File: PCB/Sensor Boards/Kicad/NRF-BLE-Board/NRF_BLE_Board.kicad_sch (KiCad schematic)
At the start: 13 parts, among them U1 nRF52805-CAxx, Y1 Crystal

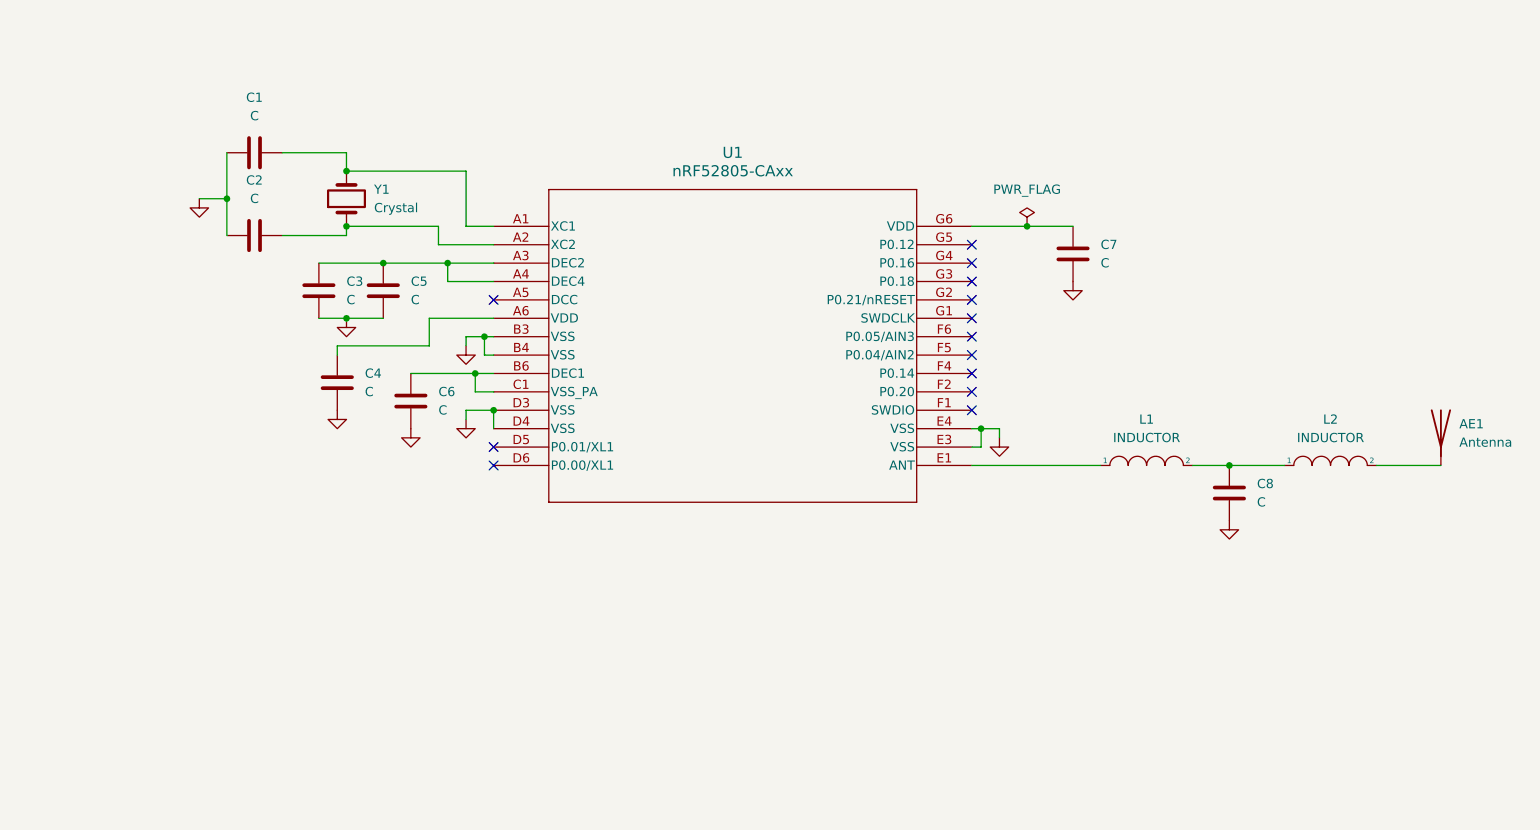
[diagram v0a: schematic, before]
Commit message: Initial placement and routing done
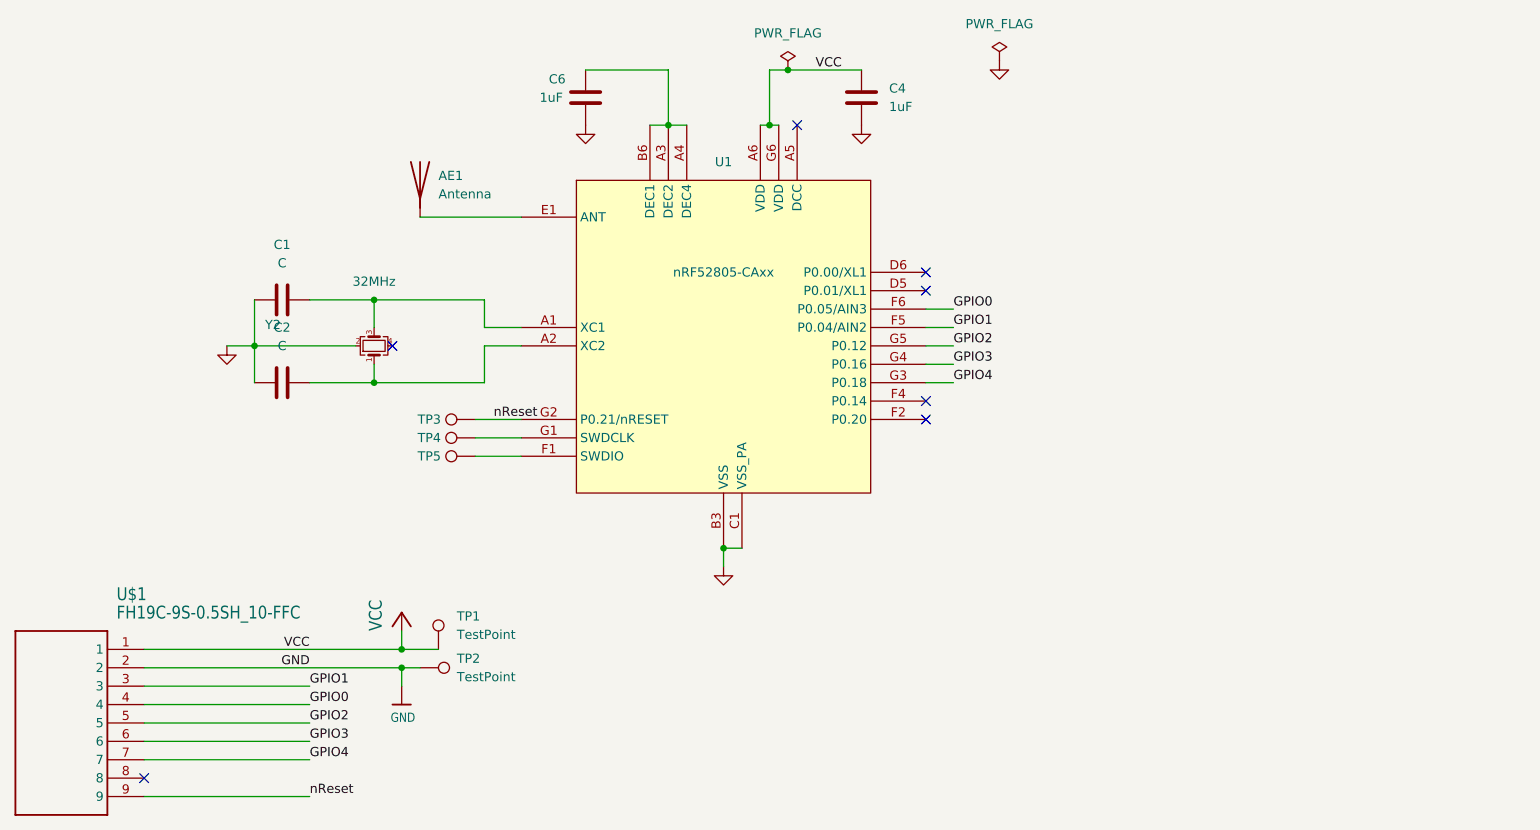
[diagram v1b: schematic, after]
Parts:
- removed C3, C5, C7, C8: C, Capacitor_SMD:C_0201_0603Metric_Pad0.64x0.40mm_HandSolder, symbol Device:C
- removed L1, L2: INDUCTOR, Inductor_SMD:L_0201_0603Metric_Pad0.64x0.40mm_HandSolder, symbol pspice:INDUCTOR
- removed Y1: Crystal, Oscillator:Oscillator_SMD_Abracon_ASCO-4Pin_1.6x1.2mm, symbol Device:Crystal
- added TP1, TP2, TP3, TP4, TP5: TestPoint, TestPoint:TestPoint_Pad_D1.0mm, symbol Connector:TestPoint
- added U$1: FH19C-9S-0.5SH_10-FFC, OSO-SWAB-B1-00 Sensor Watch Accelerometer:FH19C9S05SH10-FFC, symbol OSO-MISC-21-021 Sensor Watch Motion II-eagle-import:FH19C-9S-0.5SH_10-FFC
- added Y2: 32MHz, Crystal:Crystal_SMD_Murata_XRCTD32M000N1P1AR0-4pin_1.2x1.0mm, symbol Device:Crystal_GND24_Small
- AE1: footprint Capacitor_SMD:C_0402_1005Metric -> Capacitor_SMD:C_0402_1005Metric_Pad0.74x0.62mm_HandSolder
- C1, C2: footprint Capacitor_SMD:C_0201_0603Metric_Pad0.64x0.40mm_HandSolder -> Capacitor_SMD:C_0402_1005Metric_Pad0.74x0.62mm_HandSolder
- C4, C6: value C -> 1uF; footprint Capacitor_SMD:C_0201_0603Metric_Pad0.64x0.40mm_HandSolder -> Capacitor_SMD:C_0402_1005Metric_Pad0.74x0.62mm_HandSolder
- U1: footprint Package_CSP:NRF_WLCSP-28_2.482X2.464_NOR -> Package_CSP:NRF_WLCSP-28_2.48x2.64mm_P0.4mm
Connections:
- net GND: now also U1.C1 (VSS_PA), TP2.1, U$1.2, Y2.2
- net VCC: now reaches C4.1, U1.A6 (VDD)
- net VCC: now also U1.G6 (VDD), TP1.1, U$1.1
- net at C2.2, U1.A2 (XC2): now also Y2.1
- net at C1.2, U1.A1 (XC1): now also Y2.3
- net at U1.A3 (DEC2), U1.A4 (DEC4): now also C6.1, U1.B6 (DEC1)
- net at U1.E1 (ANT): now also AE1.1 (A)
- net at U1.F1 (SWDIO): now also TP5.1
- net GPIO1: now reaches U1.F5 (P0.04/AIN2)
- net GPIO1: now also U$1.3
- net GPIO0: now reaches U1.F6 (P0.05/AIN3)
- net GPIO0: now also U$1.4
- net at U1.G1 (SWDCLK): now also TP4.1
- net nReset: now reaches U1.G2 (P0.21/nRESET)
- net nReset: now also TP3.1, U$1.9
- net GPIO4: now reaches U1.G3 (P0.18)
- net GPIO4: now also U$1.7
- net GPIO3: now reaches U1.G4 (P0.16)
- net GPIO3: now also U$1.6
- net GPIO2: now reaches U1.G5 (P0.12)
- net GPIO2: now also U$1.5
- no-connect marks 13 -> 7
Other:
- moved on the sheet: AE1, C1, C2, C4, C6

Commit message: Routing completed
order placed at OSH Park with this gerber.
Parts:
- removed TP1, TP2, TP4, TP5: TestPoint, TestPoint:TestPoint_Pad_D1.0mm, symbol Connector:TestPoint
- added J1: Conn_01x04, TestPoint:TestPoint_4Pads_Pitch1.27mm, symbol Connector_Generic:Conn_01x04
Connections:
- net GND: now also J1.2 (Pin_2)
- net VCC: now also J1.1 (Pin_1)
- net SWDIO: now reaches U1.F1 (SWDIO)
- net SWDIO: now also J1.3 (Pin_3)
- net SWDCLK: now reaches U1.G1 (SWDCLK)
- net SWDCLK: now also J1.4 (Pin_4)
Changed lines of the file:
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@@
   (junction (at 93.98 107.95) (diameter 0) (color 0 0 0 0)
-  )
-  (junction (at 97.79 147.32) (diameter 0) (color 0 0 0 0)
-  )
-  (junction (at 97.79 144.78) (diameter 0) (color 0 0 0 0)
   )
   (junction (at 93.98 96.52) (diameter 0) (color 0 0 0 0)
@@
     (stroke (width 0) (type default))
   )
-  (wire (pts (xy 107.95 118.11) (xy 114.3 118.11))
+  (wire (pts (xy 100.33 118.11) (xy 114.3 118.11))
     (stroke (width 0) (type default))
   )
@@
     (stroke (width 0) (type default))
   )
+  (wire (pts (xy 69.85 120.65) (xy 74.93 120.65))
+    (stroke (width 0) (type default))
+  )
   (wire (pts (xy 85.09 165.1) (xy 62.23 165.1))
     (stroke (width 0) (type default))
@@
     (stroke (width 0) (type default))
   )
-  (wire (pts (xy 97.79 147.32) (xy 100.33 147.32))
-    (stroke (width 0) (type default))
-  )
   (wire (pts (xy 97.79 147.32) (xy 62.23 147.32))
     (stroke (width 0) (type default))
@@
     (stroke (width 0) (type default))
   )
+  (wire (pts (xy 69.85 118.11) (xy 76.2 118.11))
+    (stroke (width 0) (type default))
+  )
   (wire (pts (xy 134.62 72.39) (xy 137.16 72.39))
     (stroke (width 0) (type default))
@@
     (stroke (width 0) (type default))
   )
-  (wire (pts (xy 107.95 115.57) (xy 114.3 115.57))
+  (wire (pts (xy 100.33 115.57) (xy 114.3 115.57))
     (stroke (width 0) (type default))
   )
@@
     (stroke (width 0) (type default))
   )
-  (wire (pts (xy 102.87 144.78) (xy 97.79 144.78))
-    (stroke (width 0) (type default))
-  )
   (wire (pts (xy 77.47 102.87) (xy 77.47 107.95))
     (stroke (width 0) (type default))
   )
+  (wire (pts (xy 69.85 115.57) (xy 76.2 115.57))
+    (stroke (width 0) (type default))
+  )
   (wire (pts (xy 85.09 107.95) (xy 93.98 107.95))
     (stroke (width 0) (type default))
@@
     (stroke (width 0) (type default))
   )
+  (wire (pts (xy 69.85 123.19) (xy 74.93 123.19))
+    (stroke (width 0) (type default))
+  )
   (wire (pts (xy 148.59 72.39) (xy 149.86 72.39))
     (stroke (width 0) (type default))
@@
     (effects (font (size 1.27 1.27)) (justify left bottom))
   )
+  (label "VCC" (at 74.93 123.19 180) (fields_autoplaced)
+    (effects (font (size 1.2446 1.2446)) (justify right bottom))
+  )
   (label "GPIO1" (at 85.09 149.86 0) (fields_autoplaced)
     (effects (font (size 1.27 1.27)) (justify left bottom))
@@
     (effects (font (size 1.27 1.27)) (justify left bottom))
   )
+  (label "SWDIO" (at 100.33 118.11 0) (fields_autoplaced)
+    (effects (font (size 1 1)) (justify left bottom))
+  )
+  (label "SWDCLK" (at 100.33 115.57 0) (fields_autoplaced)
+    (effects (font (size 1 1)) (justify left bottom))
+  )
   (label "GPIO0" (at 173.99 97.79 0) (fields_autoplaced)
     (effects (font (size 1.27 1.27)) (justify left bottom))
+  )
+  (label "SWDIO" (at 76.2 118.11 180) (fields_autoplaced)
+    (effects (font (size 1 1)) (justify right bottom))
+  )
+  (label "GND" (at 74.93 120.65 180) (fields_autoplaced)
+    (effects (font (size 1.2446 1.2446)) (justify right bottom))
   )
   (label "nReset" (at 85.09 165.1 0) (fields_autoplaced)
@@
   (label "GND" (at 85.09 147.32 180) (fields_autoplaced)
     (effects (font (size 1.2446 1.2446)) (justify right bottom))
+  )
+  (label "SWDCLK" (at 76.2 115.57 180) (fields_autoplaced)
+    (effects (font (size 1 1)) (justify right bottom))
   )
   (label "GPIO0" (at 85.09 152.4 0) (fields_autoplaced)
@@
     )
   )
-  (symbol (lib_id "Connector:TestPoint") (at 100.33 147.32 270) (unit 1)
-    (in_bom yes) (on_board yes) (dnp no) (fields_autoplaced)
-    (property "Reference" "TP2" (at 105.41 146.05 90)
-      (effects (font (size 1.27 1.27)) (justify left))
-    )
-    (property "Value" "TestPoint" (at 105.41 148.59 90)
-      (effects (font (size 1.27 1.27)) (justify left))
-    )
-    (property "Footprint" "TestPoint:TestPoint_Pad_D1.0mm" (at 100.33 152.4 0)
-      (effects (font (size 1.27 1.27)) hide)
-    )
-    (property "Datasheet" "~" (at 100.33 152.4 0)
-      (effects (font (size 1.27 1.27)) hide)
-    )
-    (pin "1")
-    (instances
-      (project "NRF_BLE_Board"
-        (path "/34b18e33-c413-4b44-9f16-855bb8aeab29"
-          (reference "TP2") (unit 1)
-        )
-      )
-    )
-  )
   (symbol (lib_id "power:PWR_FLAG") (at 151.13 64.77 0) (unit 1)
     (in_bom yes) (on_board yes) (dnp no) (fields_autoplaced)
@@
         (path "/34b18e33-c413-4b44-9f16-855bb8aeab29"
           (reference "#FLG01") (unit 1)
-        )
-      )
-    )
-  )
-  (symbol (lib_id "Connector:TestPoint") (at 107.95 118.11 90) (unit 1)
-    (in_bom yes) (on_board yes) (dnp no)
-    (property "Reference" "TP5" (at 101.6 118.11 90)
-      (effects (font (size 1.27 1.27)))
-    )
-    (property "Value" "TestPoint" (at 104.648 115.57 90)
-      (effects (font (size 1.27 1.27)) hide)
-    )
-    (property "Footprint" "TestPoint:TestPoint_Pad_D1.0mm" (at 107.95 113.03 0)
-      (effects (font (size 1.27 1.27)) hide)
-    )
-    (property "Datasheet" "~" (at 107.95 113.03 0)
-      (effects (font (size 1.27 1.27)) hide)
-    )
-    (pin "1")
-    (instances
-      (project "NRF_BLE_Board"
-        (path "/34b18e33-c413-4b44-9f16-855bb8aeab29"
-          (reference "TP5") (unit 1)
         )
       )
@@
     )
   )
-  (symbol (lib_id "Connector:TestPoint") (at 107.95 115.57 90) (unit 1)
-    (in_bom yes) (on_board yes) (dnp no)
-    (property "Reference" "TP4" (at 101.6 115.57 90)
-      (effects (font (size 1.27 1.27)))
-    )
-    (property "Value" "TestPoint" (at 104.648 113.03 90)
-      (effects (font (size 1.27 1.27)) hide)
-    )
-    (property "Footprint" "TestPoint:TestPoint_Pad_D1.0mm" (at 107.95 110.49 0)
-      (effects (font (size 1.27 1.27)) hide)
-    )
-    (property "Datasheet" "~" (at 107.95 110.49 0)
-      (effects (font (size 1.27 1.27)) hide)
-    )
-    (pin "1")
-    (instances
-      (project "NRF_BLE_Board"
-        (path "/34b18e33-c413-4b44-9f16-855bb8aeab29"
-          (reference "TP4") (unit 1)
+  (symbol (lib_id "Connector_Generic:Conn_01x04") (at 64.77 120.65 180) (unit 1)
+    (in_bom yes) (on_board yes) (dnp no) (fields_autoplaced)
+    (property "Reference" "J1" (at 64.77 109.22 0)
+      (effects (font (size 1.27 1.27)))
+    )
+    (property "Value" "Conn_01x04" (at 64.77 111.76 0)
+      (effects (font (size 1.27 1.27)))
+    )
+    (property "Footprint" "TestPoint:TestPoint_4Pads_Pitch1.27mm" (at 64.77 120.65 0)
+      (effects (font (size 1.27 1.27)) hide)
+    )
+    (property "Datasheet" "~" (at 64.77 120.65 0)
+      (effects (font (size 1.27 1.27)) hide)
+    )
+    (pin "1")
+    (pin "2")
+    (pin "3")
+    (pin "4")
+    (instances
+      (project "NRF_BLE_Board"
+        (path "/34b18e33-c413-4b44-9f16-855bb8aeab29"
+          (reference "J1") (unit 1)
         )
       )
@@
         )
       )
-    )
-  )
-  (symbol (lib_id "Connector:TestPoint") (at 102.87 144.78 0) (unit 1)
-    (in_bom yes) (on_board yes) (dnp no) (fields_autoplaced)
-    (property "Reference" "TP1" (at 105.41 140.208 0)
-      (effects (font (size 1.27 1.27)) (justify left))
-    )
-    (property "Value" "TestPoint" (at 105.41 142.748 0)
-      (effects (font (size 1.27 1.27)) (justify left))
-    )
-    (property "Footprint" "TestPoint:TestPoint_Pad_D1.0mm" (at 107.95 144.78 0)
-      (effects (font (size 1.27 1.27)) hide)
-    )
-    (property "Datasheet" "~" (at 107.95 144.78 0)
-      (effects (font (size 1.27 1.27)) hide)
-    )
-    (pin "1")
-    (instances
-      (project "NRF_BLE_Board"
-        (path "/34b18e33-c413-4b44-9f16-855bb8aeab29"
-          (reference "TP1") (unit 1)
-        )
-      )

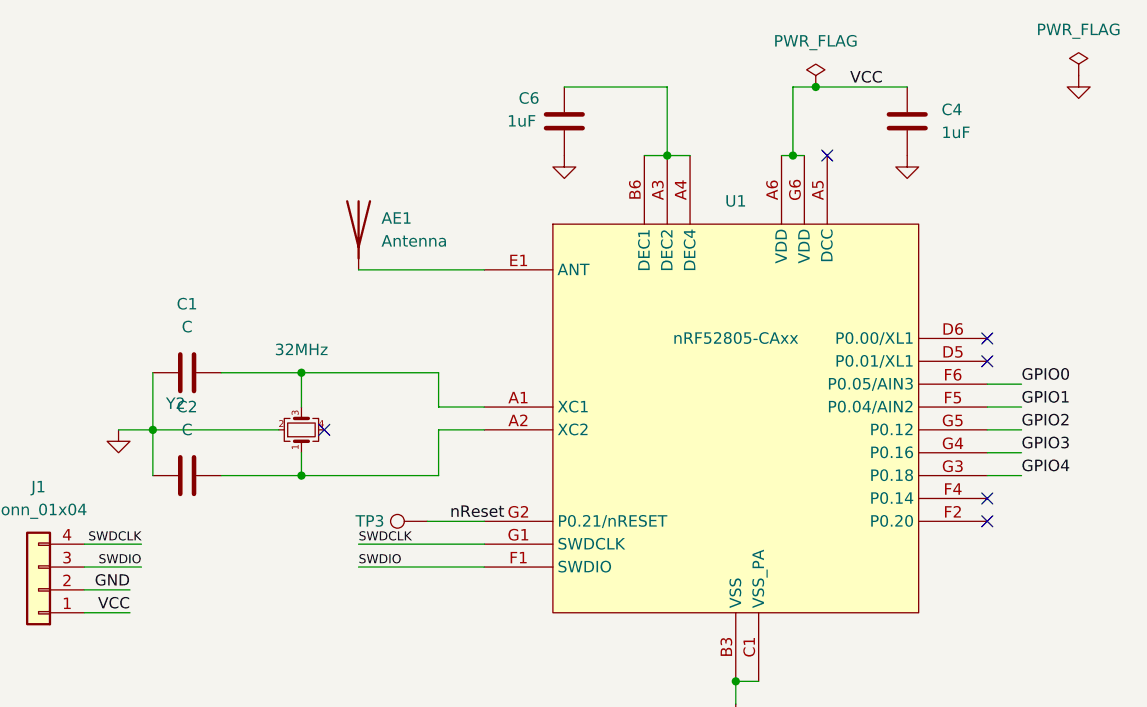
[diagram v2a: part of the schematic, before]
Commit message: Add component values and other cleanup
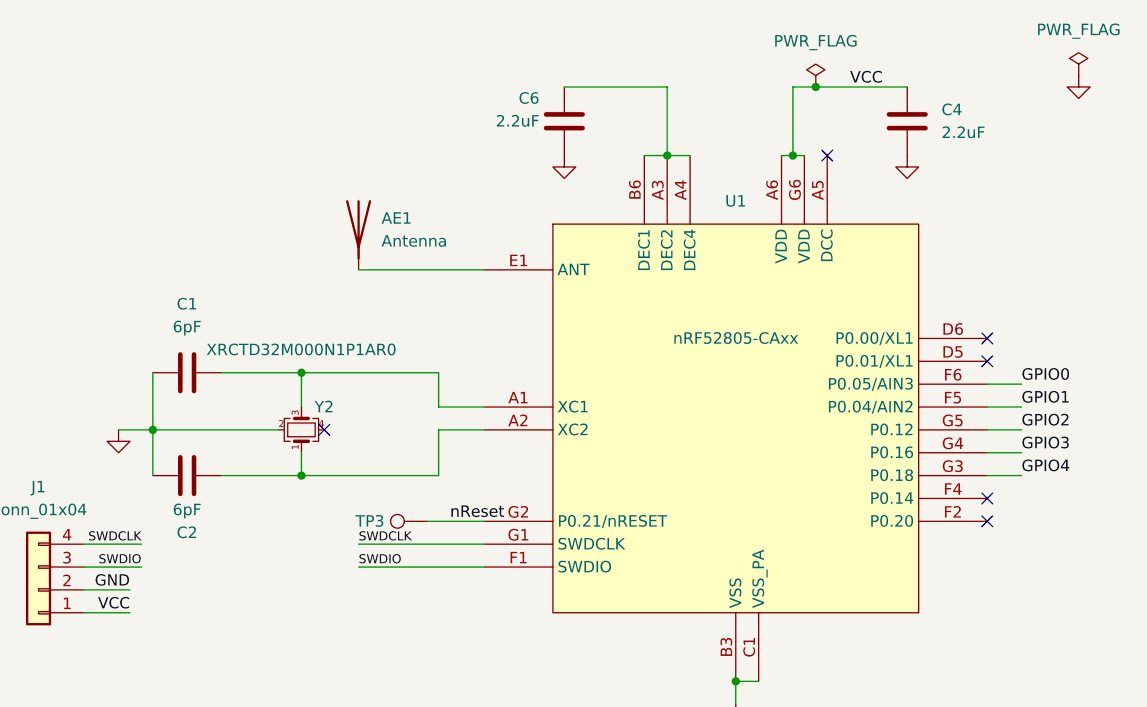
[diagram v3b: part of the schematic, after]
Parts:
- C1, C2: value C -> 6pF
- C4, C6: value 1uF -> 2.2uF
- Y2: value 32MHz -> XRCTD32M000N1P1AR0
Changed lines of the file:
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@@
   (symbol (lib_id "Device:C") (at 161.29 68.58 0) (unit 1)
     (in_bom yes) (on_board yes) (dnp no) (fields_autoplaced)
-    (property "Reference" "C4" (at 165.1 67.3099 0)
-      (effects (font (size 1.27 1.27)) (justify left))
-    )
-    (property "Value" "1uF" (at 165.1 69.8499 0)
+    (property "Reference" "C4" (at 165.1 67.31 0)
+      (effects (font (size 1.27 1.27)) (justify left))
+    )
+    (property "Value" "2.2uF" (at 165.1 69.85 0)
       (effects (font (size 1.27 1.27)) (justify left))
     )
@@
   )
   (symbol (lib_id "Device:C") (at 81.28 107.95 90) (unit 1)
-    (in_bom yes) (on_board yes) (dnp no) (fields_autoplaced)
-    (property "Reference" "C2" (at 81.28 100.33 90)
-      (effects (font (size 1.27 1.27)))
-    )
-    (property "Value" "C" (at 81.28 102.87 90)
+    (in_bom yes) (on_board yes) (dnp no)
+    (property "Reference" "C2" (at 81.28 114.3 90)
+      (effects (font (size 1.27 1.27)))
+    )
+    (property "Value" "6pF" (at 81.28 111.76 90)
       (effects (font (size 1.27 1.27)))
     )
@@
       (effects (font (size 1.27 1.27)) (justify left))
     )
-    (property "Value" "1uF" (at 116.84 68.58 0)
+    (property "Value" "2.2uF" (at 115.57 68.58 0)
       (effects (font (size 1.27 1.27)) (justify left))
     )
@@
   (symbol (lib_id "Device:Crystal_GND24_Small") (at 93.98 102.87 270) (mirror x) (unit 1)
     (in_bom yes) (on_board yes) (dnp no)
-    (property "Reference" "Y2" (at 80.01 99.9557 90)
-      (effects (font (size 1.27 1.27)))
-    )
-    (property "Value" "32MHz" (at 93.98 93.98 90)
+    (property "Reference" "Y2" (at 96.52 100.33 90)
+      (effects (font (size 1.27 1.27)))
+    )
+    (property "Value" "XRCTD32M000N1P1AR0" (at 93.98 93.98 90)
       (effects (font (size 1.27 1.27)))
     )
@@
       (effects (font (size 1.27 1.27)))
     )
-    (property "Value" "C" (at 81.28 91.44 90)
-      (effects (font (size 1.27 1.27)))
-    )
+    (property "Value" "6pF" (at 81.28 91.44 90)
+      (effects (font (size 1.27 1.27)))
+    )
